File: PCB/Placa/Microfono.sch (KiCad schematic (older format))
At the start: 12 parts, among them U9 OPA2335

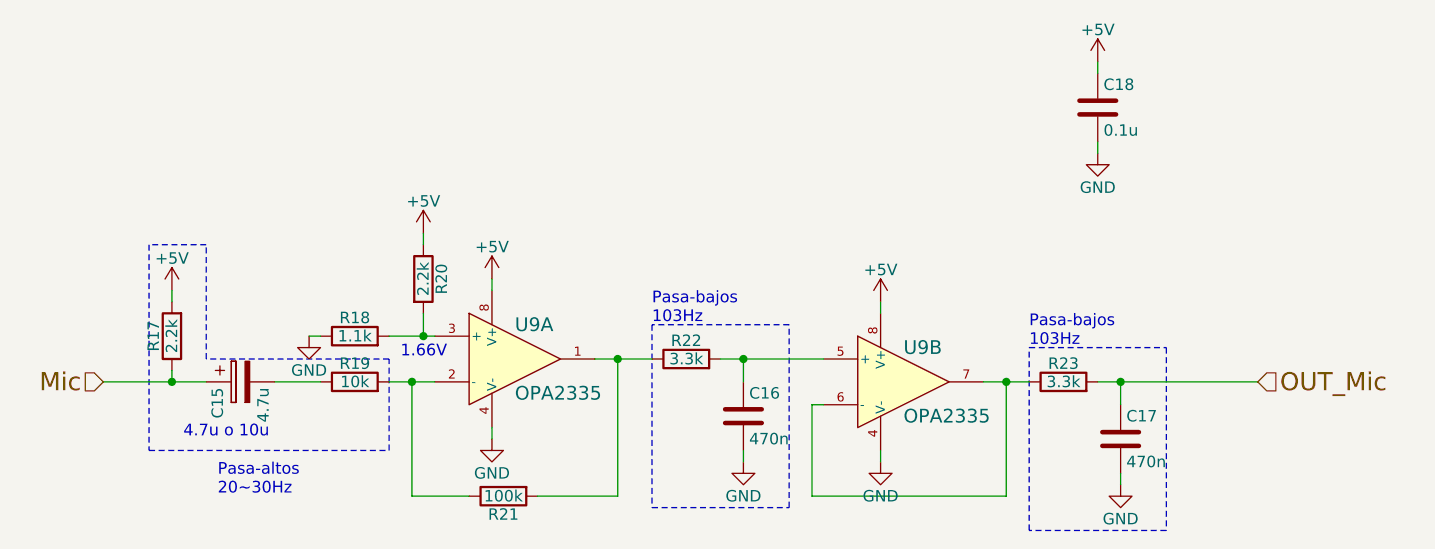
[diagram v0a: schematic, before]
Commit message: Modifiqué la placa. Le agregué la resistencia para el divisor a la salida del micrófono y cambié la frecuencia del pasabajos a 500Hz aprox, por lo que estuvimos hablando con Mario.
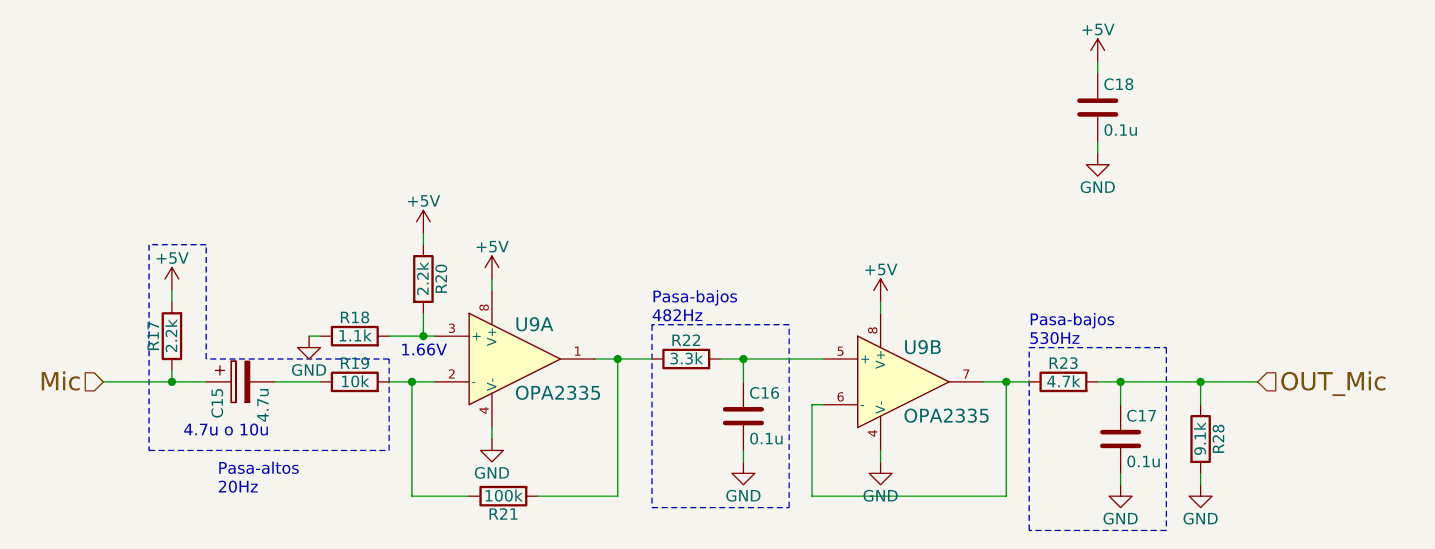
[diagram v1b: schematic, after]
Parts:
- added R28: 9.1k, Resistors_SMD:R_0805, symbol R
- C16, C17: value 470n -> 0.1u
- R23: value 3.3k -> 4.7k
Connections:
- net GND: now also R28.2
- net OUT_Mic: now also R28.1
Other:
- note added: "Pasa-altos\n20Hz"
- note added: "Pasa-bajos\n482Hz"
- note added: "Pasa-bajos\n530Hz"
- note removed: "Pasa-altos\n20~~30Hz"
- note removed: "Pasa-bajos\n103Hz"
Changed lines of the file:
@@
 P 5850 3950
 F 0 "C16" H 5875 4050 50  0000 L CNN
-F 1 "470n" H 5875 3850 50  0000 L CNN
+F 1 "0.1u" H 5875 3850 50  0000 L CNN
 F 2 "Capacitors_SMD:C_0805" H 5888 3800 50  0001 C CNN
 F 3 "" H 5850 3950 50  0000 C CNN
@@
 P 7250 3800
 F 0 "R23" V 7330 3800 50  0000 C CNN
-F 1 "3.3k" V 7250 3800 50  0000 C CNN
+F 1 "4.7k" V 7250 3800 50  0000 C CNN
 F 2 "Resistors_SMD:R_0805" V 7180 3800 30  0001 C CNN
 F 3 "" H 7250 3800 30  0000 C CNN
@@
 P 7500 4050
 F 0 "C17" H 7525 4150 50  0000 L CNN
-F 1 "470n" H 7525 3950 50  0000 L CNN
+F 1 "0.1u" H 7525 3950 50  0000 L CNN
 F 2 "Capacitors_SMD:C_0805" H 7538 3900 50  0001 C CNN
 F 3 "" H 7500 4050 50  0000 C CNN
@@
 	3500 3200 3250 3200
 Text Notes 3550 4300 0    51   ~ 0
-Pasa-altos\n20~~30Hz
+Pasa-altos\n20Hz
 Wire Notes Line
 	5450 3550 5450 4350
@@
 	7100 4450 7100 3650
 Text Notes 5450 3550 0    51   ~ 0
-Pasa-bajos\n103Hz
+Pasa-bajos\n482Hz
 Text Notes 7100 3650 0    51   ~ 0
-Pasa-bajos\n103Hz
+Pasa-bajos\n530Hz
 $Comp
 L C C18
@@
 Text HLabel 8100 3800 2    79   Input ~ 0
 OUT_Mic
+$Comp
+L R R28
+U 1 1 571E83A5
+P 7850 4050
+F 0 "R28" V 7930 4050 50  0000 C CNN
+F 1 "9.1k" V 7850 4050 50  0000 C CNN
+F 2 "Resistors_SMD:R_0805" V 7780 4050 30  0001 C CNN
+F 3 "" H 7850 4050 30  0000 C CNN
+	1    7850 4050
+	1    0    0    -1
+$EndComp
+Wire Wire Line
+	7850 3900 7850 3800
+Connection ~ 7850 3800
+Wire Wire Line
+	7850 4200 7850 4250
+$Comp
+L GND #PWR047
+U 1 1 571E853F
+P 7850 4250
+F 0 "#PWR047" H 7850 4000 50  0001 C CNN
+F 1 "GND" H 7850 4100 50  0000 C CNN
+F 2 "" H 7850 4250 60  0000 C CNN
+F 3 "" H 7850 4250 60  0000 C CNN
+	1    7850 4250
+	1    0    0    -1
+$EndComp
 $EndSCHEMATC

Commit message: Recalculé unas resistencias porque consigo de la serie E12
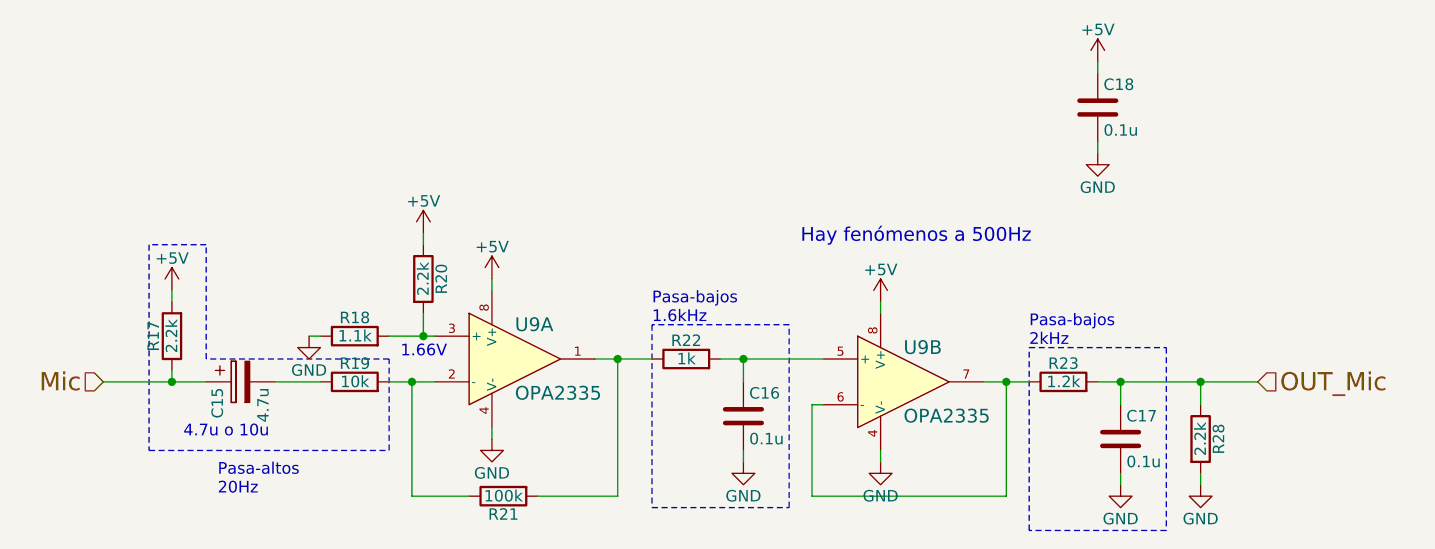
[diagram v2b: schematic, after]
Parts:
- R22: value 3.3k -> 1k
- R23: value 4.7k -> 1.2k
- R28: value 9.1k -> 2.2k
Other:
- note added: "Hay fenómenos a 500Hz"
- note added: "Pasa-bajos\n1.6kHz"
- note added: "Pasa-bajos\n2kHz"
- note removed: "Pasa-bajos\n482Hz"
- note removed: "Pasa-bajos\n530Hz"
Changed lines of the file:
@@
 P 5600 3700
 F 0 "R22" V 5680 3700 50  0000 C CNN
-F 1 "3.3k" V 5600 3700 50  0000 C CNN
+F 1 "1k" V 5600 3700 50  0000 C CNN
 F 2 "Resistors_SMD:R_0805" V 5530 3700 30  0001 C CNN
 F 3 "" H 5600 3700 30  0000 C CNN
@@
 P 7250 3800
 F 0 "R23" V 7330 3800 50  0000 C CNN
-F 1 "4.7k" V 7250 3800 50  0000 C CNN
+F 1 "1.2k" V 7250 3800 50  0000 C CNN
 F 2 "Resistors_SMD:R_0805" V 7180 3800 30  0001 C CNN
 F 3 "" H 7250 3800 30  0000 C CNN
@@
 	7100 4450 7100 3650
 Text Notes 5450 3550 0    51   ~ 0
-Pasa-bajos\n482Hz
+Pasa-bajos\n1.6kHz
 Text Notes 7100 3650 0    51   ~ 0
-Pasa-bajos\n530Hz
+Pasa-bajos\n2kHz
 $Comp
 L C C18
@@
 P 7850 4050
 F 0 "R28" V 7930 4050 50  0000 C CNN
-F 1 "9.1k" V 7850 4050 50  0000 C CNN
+F 1 "2.2k" V 7850 4050 50  0000 C CNN
 F 2 "Resistors_SMD:R_0805" V 7780 4050 30  0001 C CNN
 F 3 "" H 7850 4050 30  0000 C CNN
@@
 	1    0    0    -1
 $EndComp
+Text Notes 6100 3200 0    60   ~ 0
+Hay fenómenos a 500Hz
 $EndSCHEMATC
